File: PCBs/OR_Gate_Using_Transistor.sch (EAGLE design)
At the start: 11 parts, among them T1 2N3904, T2 2N3904

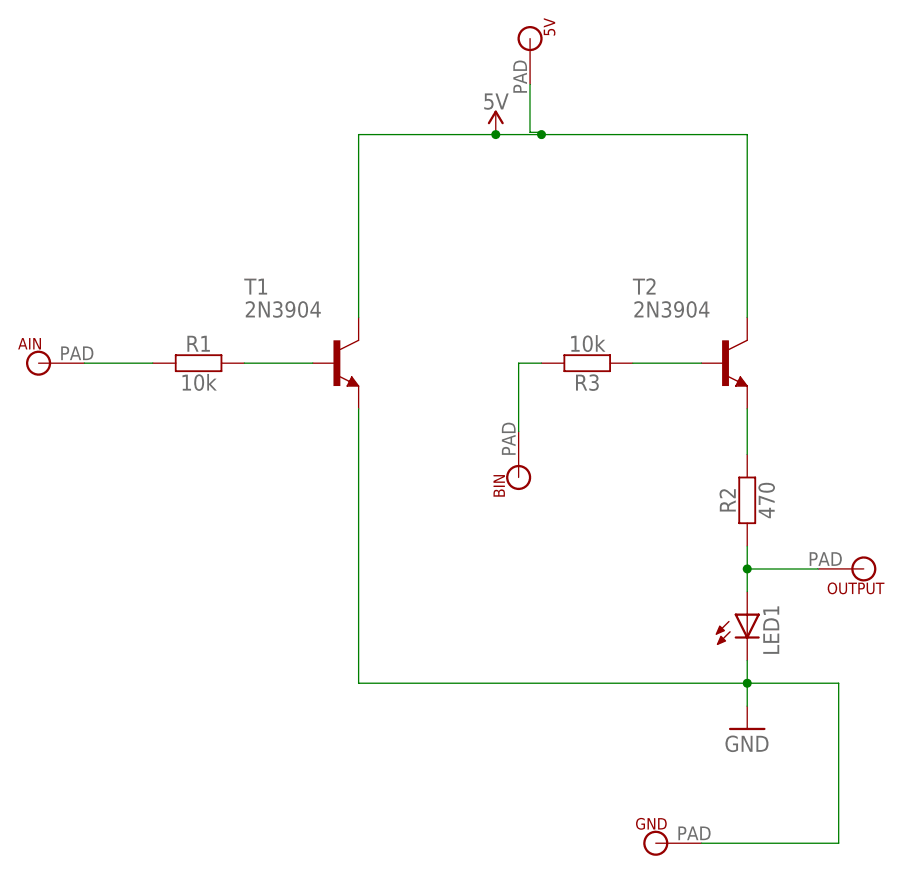
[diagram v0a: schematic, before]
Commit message: Update for Dim width is 42 length is 28 for type 2 pcb
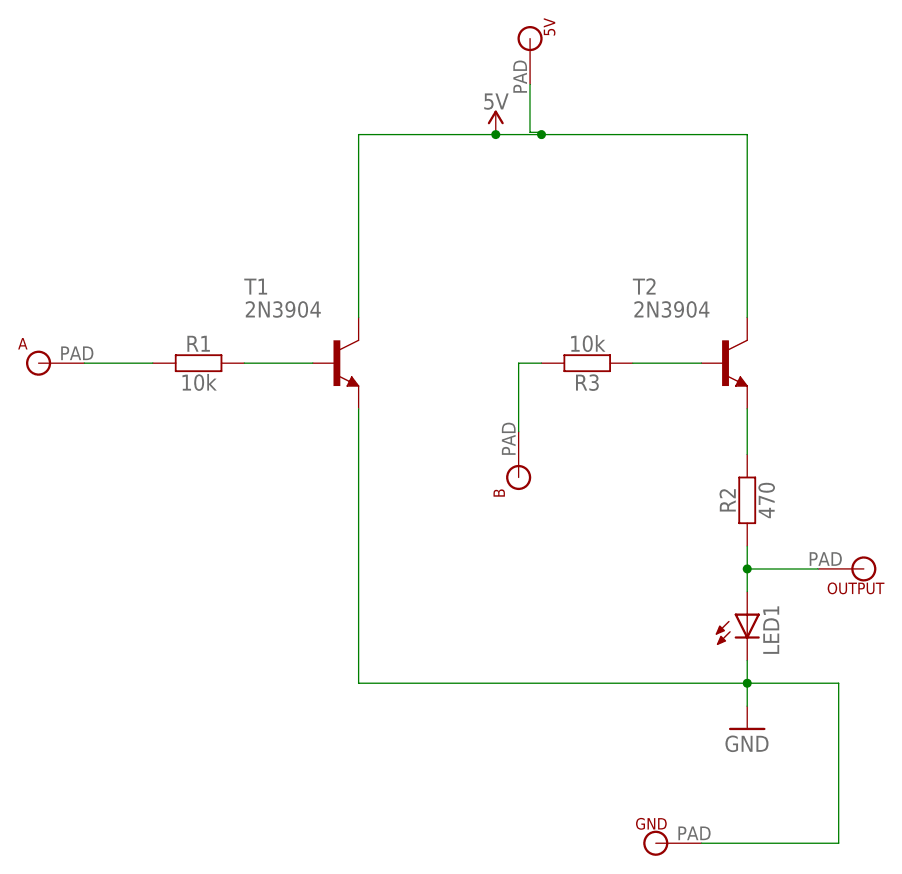
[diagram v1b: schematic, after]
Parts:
- renumbered AIN to A, BIN to B
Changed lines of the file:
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@@
 <part name="SUPPLY1" library="SparkFun-PowerSymbols" library_urn="urn:adsk.eagle:library:530" deviceset="5V" device=""/>
 <part name="GND1" library="supply1" library_urn="urn:adsk.eagle:library:371" deviceset="GND" device=""/>
-<part name="BIN" library="microbit" deviceset="MICROBIT_PAD" device=""/>
-<part name="AIN" library="microbit" deviceset="MICROBIT_PAD" device=""/>
+<part name="B" library="microbit" deviceset="MICROBIT_PAD" device=""/>
+<part name="A" library="microbit" deviceset="MICROBIT_PAD" device=""/>
 <part name="5V" library="microbit" deviceset="MICROBIT_PAD" device=""/>
 <part name="OUTPUT" library="microbit" deviceset="MICROBIT_PAD" device=""/>
@@
 <attribute name="VALUE" x="76.2" y="15.24" size="1.778" layer="96"/>
 </instance>
-<instance part="BIN" gate="G$1" x="53.34" y="45.72" smashed="yes" rot="R90">
+<instance part="B" gate="G$1" x="53.34" y="45.72" smashed="yes" rot="R90">
 <attribute name="NAME" x="51.816" y="43.434" size="1.27" layer="94" rot="R90"/>
 </instance>
-<instance part="AIN" gate="G$1" x="0" y="58.42" smashed="yes">
+<instance part="A" gate="G$1" x="0" y="58.42" smashed="yes">
 <attribute name="NAME" x="-2.286" y="59.944" size="1.27" layer="94"/>
 </instance>
@@
 <net name="N$2" class="0">
 <segment>
-<pinref part="BIN" gate="G$1" pin="P$1"/>
+<pinref part="B" gate="G$1" pin="P$1"/>
 <pinref part="R3" gate="R" pin="2"/>
 <wire x1="53.34" y1="50.8" x2="53.34" y2="58.42" width="0.1524" layer="91"/>
@@
 <net name="N$5" class="0">
 <segment>
-<pinref part="AIN" gate="G$1" pin="P$1"/>
+<pinref part="A" gate="G$1" pin="P$1"/>
 <pinref part="R1" gate="R" pin="1"/>
 <wire x1="5.08" y1="58.42" x2="12.7" y2="58.42" width="0.1524" layer="91"/>
